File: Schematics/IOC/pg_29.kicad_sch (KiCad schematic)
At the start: 18 parts, among them U2901 F374, U2902 F374, U2903 F374, U2904 F374, U2905 F280, U2906 F280, U2907 F280, U2908 F280, U2909 F374, U2910 F20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

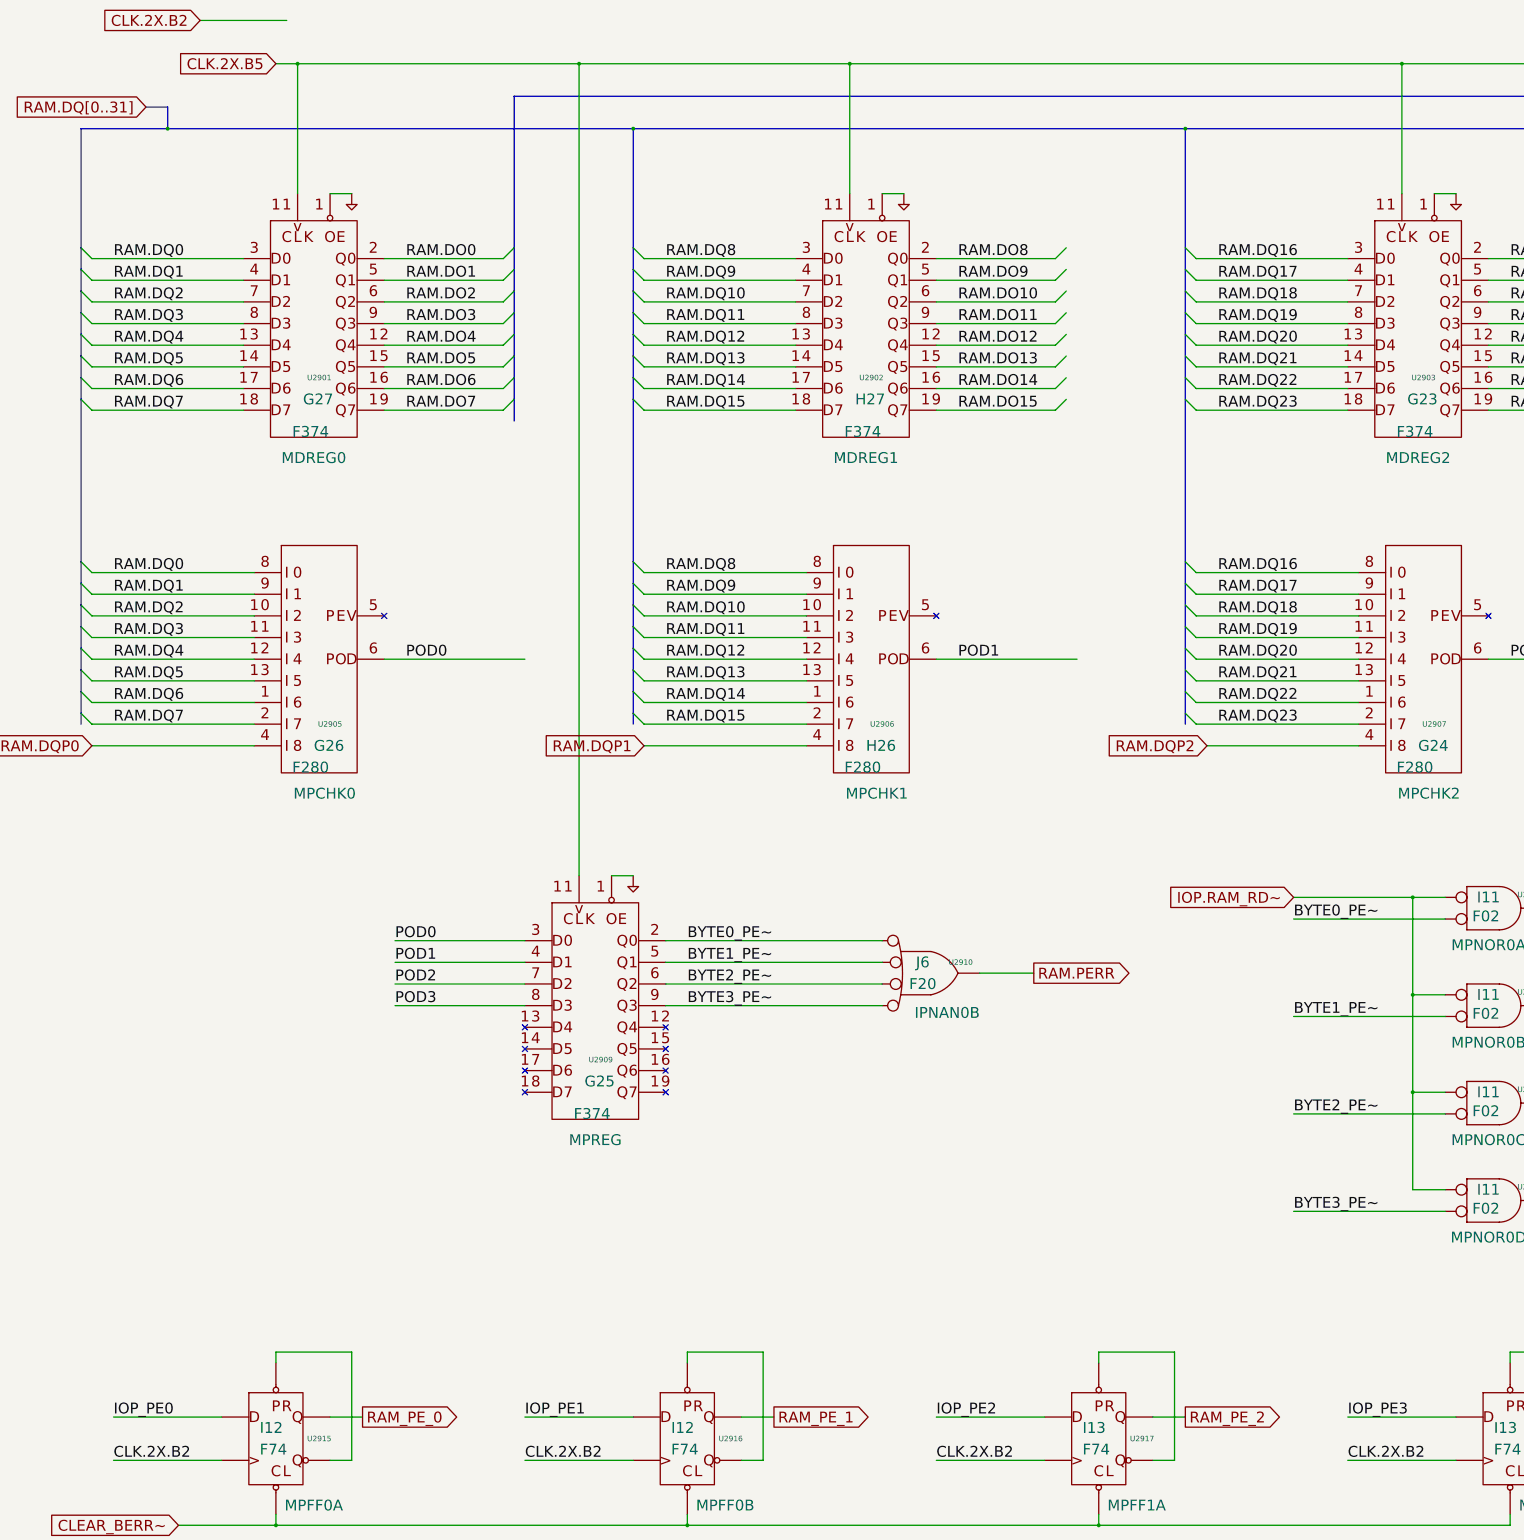
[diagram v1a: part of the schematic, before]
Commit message: Eliminate all multi-buffered signals
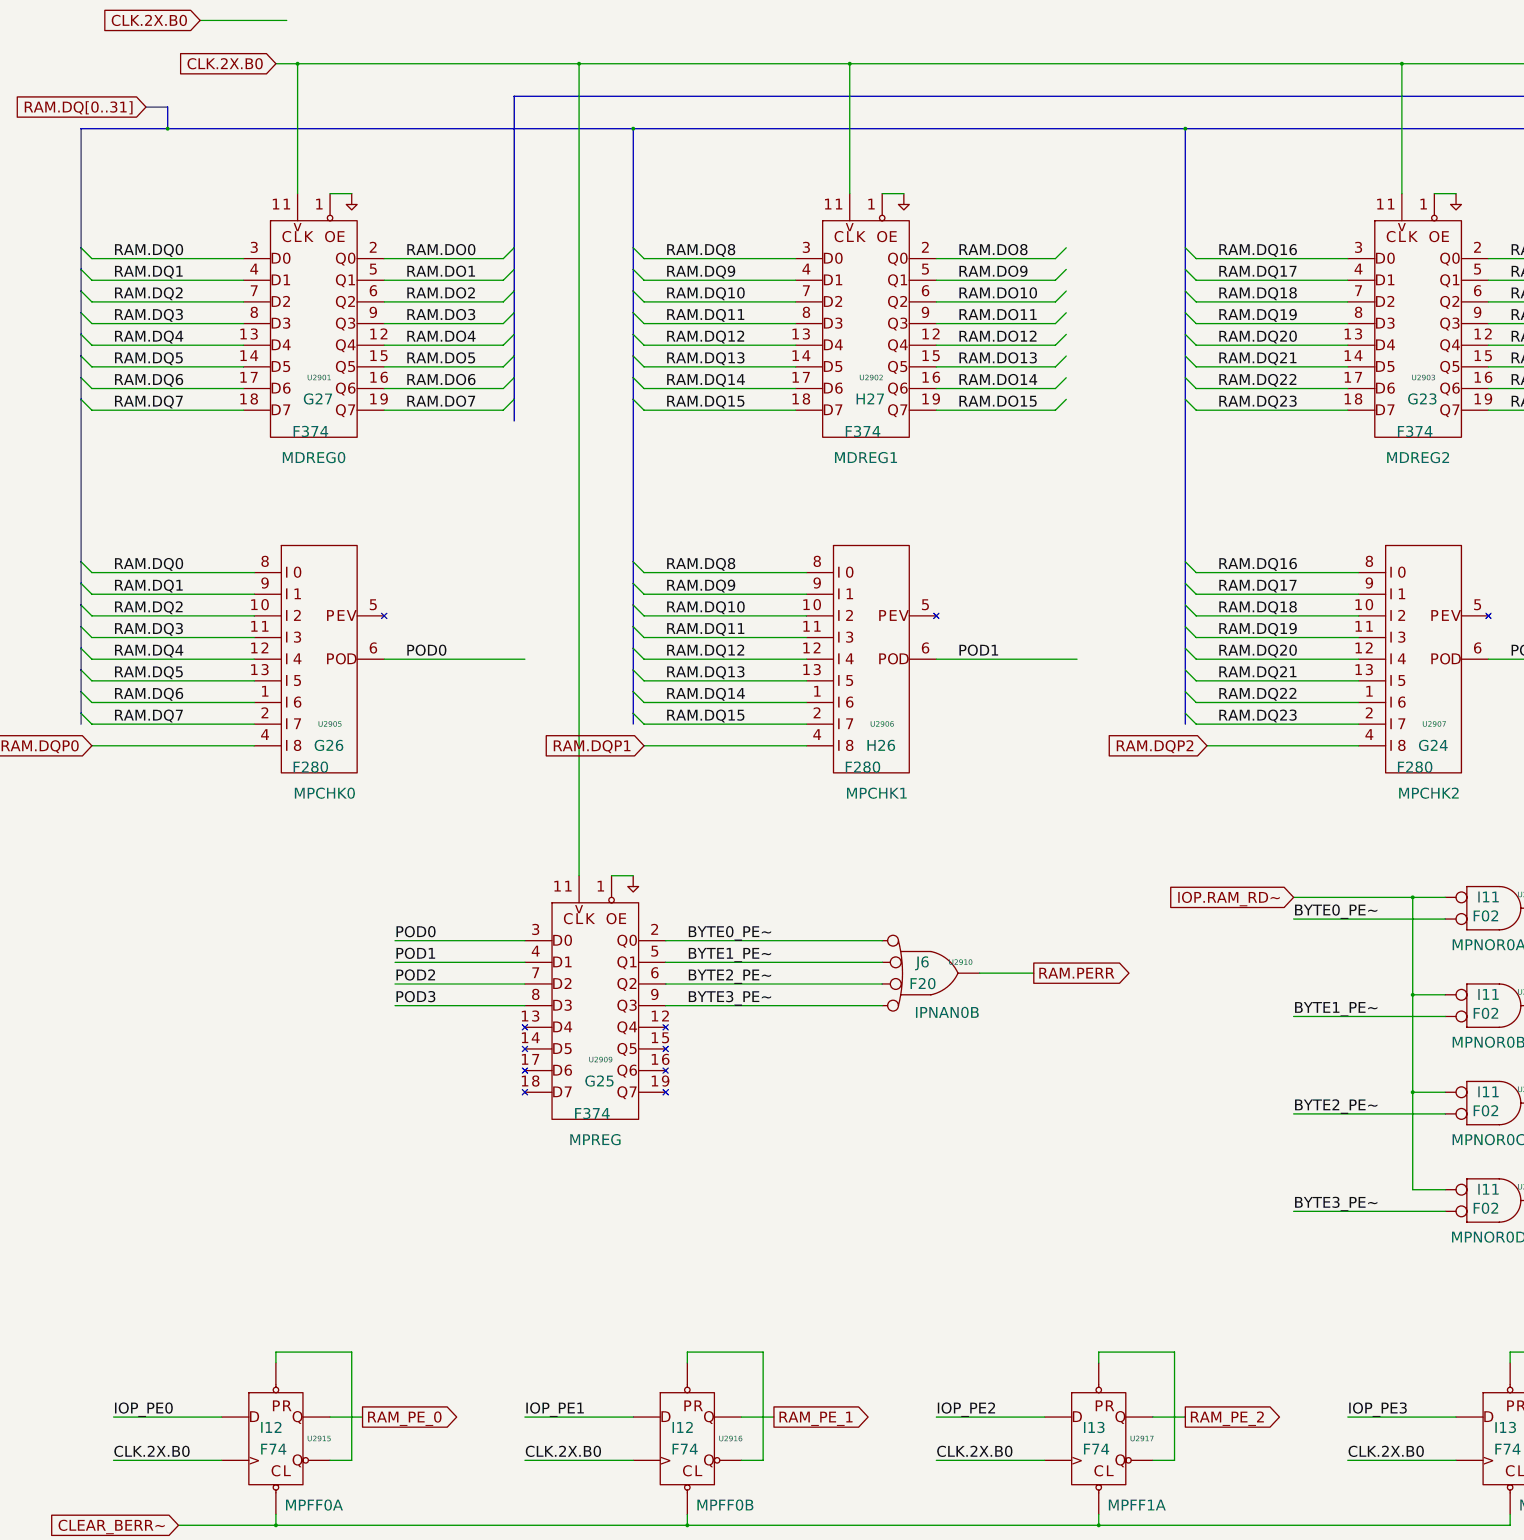
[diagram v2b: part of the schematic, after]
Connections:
- net CLK.2X.B5 is gone; now on net CLK.2X.B0: U2901.11 (CLK), U2902.11 (CLK), U2903.11 (CLK), U2904.11 (CLK), U2909.11 (CLK)
- net CLK.2X.B2 renamed CLK.2X.B0
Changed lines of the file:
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@@
   )
   (label
-    "CLK.2X.B2"
+    "CLK.2X.B0"
     (at 332.74 350.52 0)
     (effects
@@
   )
   (label
-    "CLK.2X.B2"
+    "CLK.2X.B0"
     (at 139.7 350.52 0)
     (effects
@@
   )
   (label
-    "CLK.2X.B2"
+    "CLK.2X.B0"
     (at 236.22 350.52 0)
     (effects
@@
   )
   (label
-    "CLK.2X.B2"
+    "CLK.2X.B0"
     (at 43.18 350.52 0)
     (effects
@@
   )
   (global_label
-    "CLK.2X.B5"
+    "CLK.2X.B0"
     (shape input)
     (at 81.28 22.86 180)
@@
   )
   (global_label
-    "CLK.2X.B2"
+    "CLK.2X.B0"
     (shape input)
     (at 63.5 12.7 180)

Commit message: Replace lots of clock-generation logic with CLKGEN
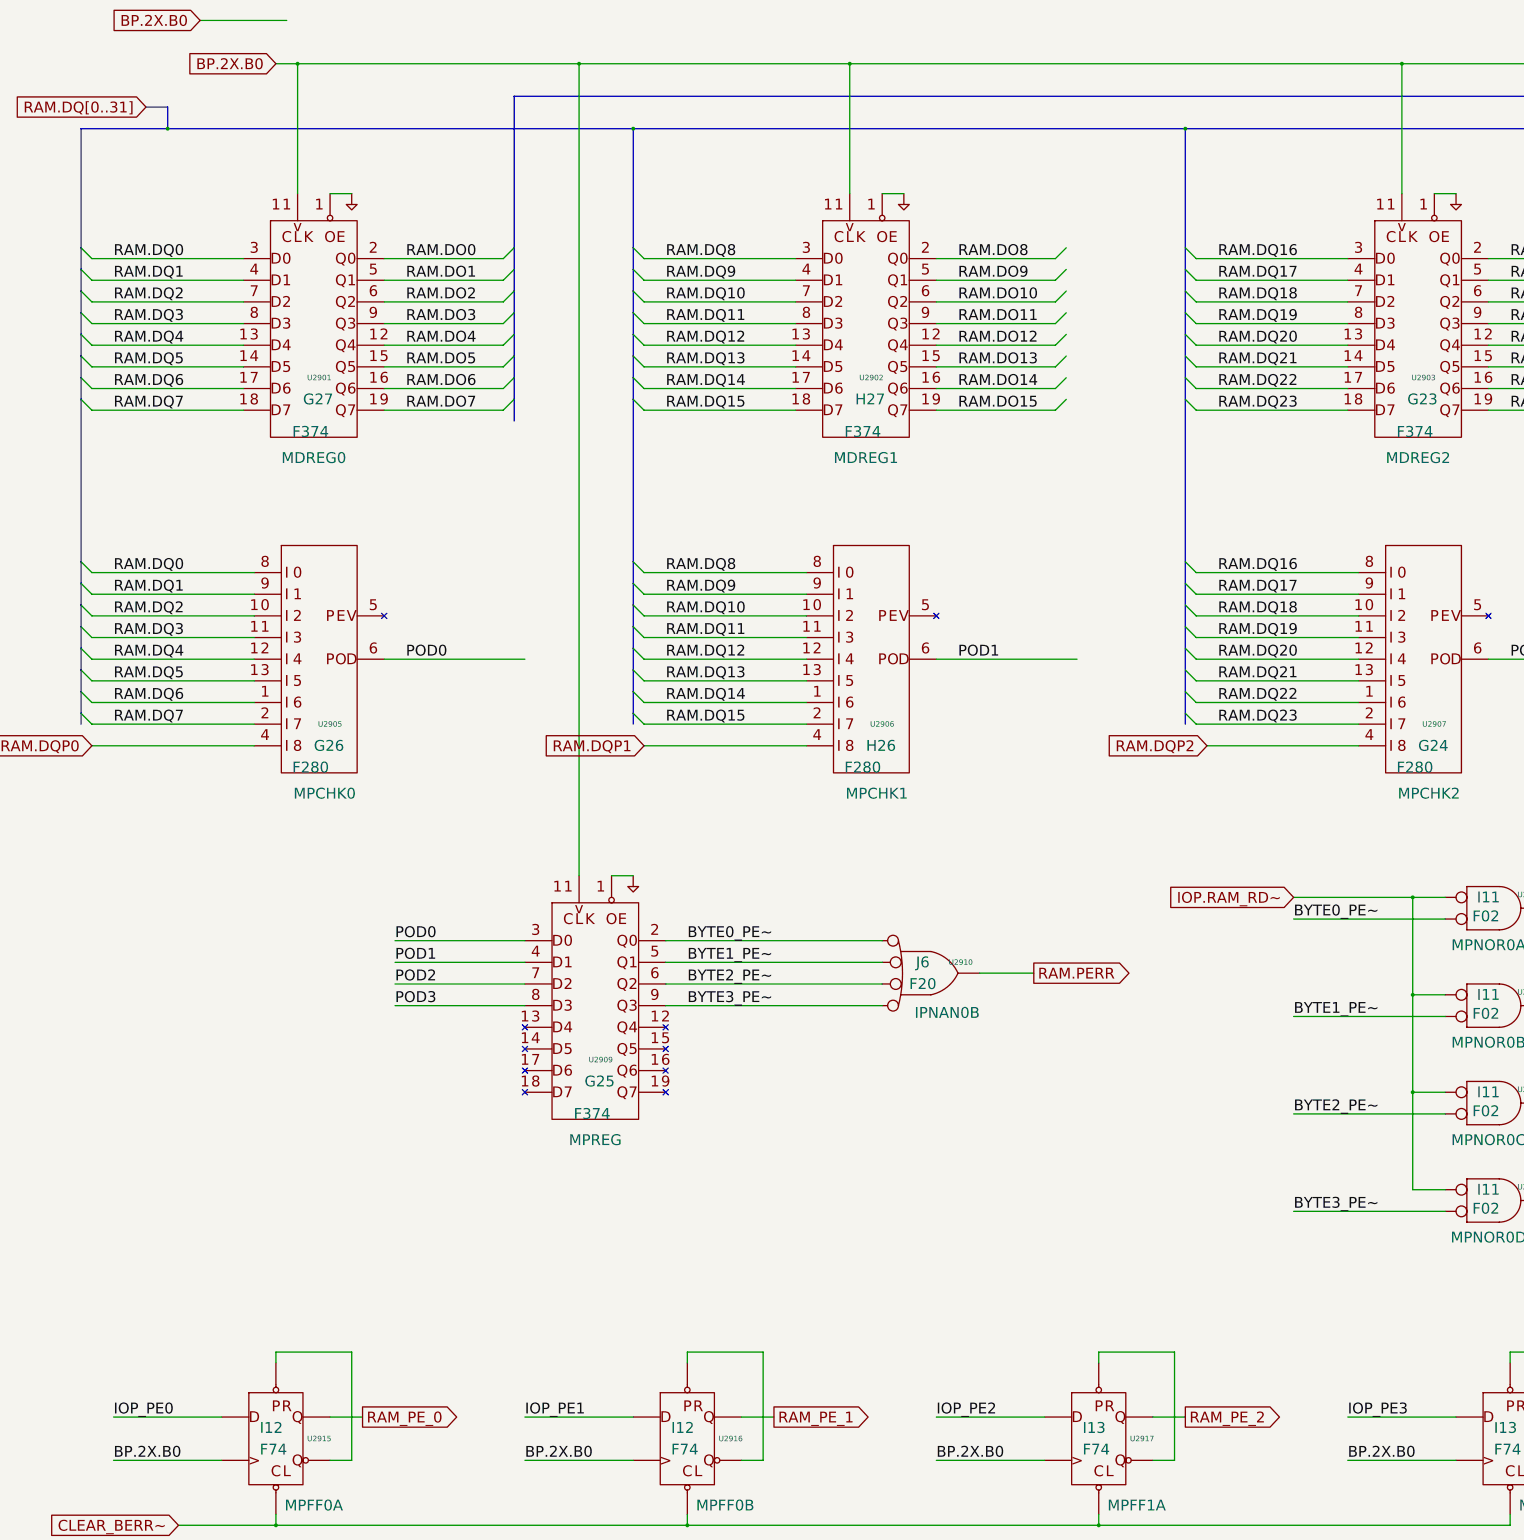
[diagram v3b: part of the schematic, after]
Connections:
- net CLK.2X.B0 renamed BP.2X.B0
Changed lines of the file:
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@@
   )
   (label
-    "CLK.2X.B0"
+    "BP.2X.B0"
     (at 332.74 350.52 0)
     (effects
@@
   )
   (label
-    "CLK.2X.B0"
+    "BP.2X.B0"
     (at 139.7 350.52 0)
     (effects
@@
   )
   (label
-    "CLK.2X.B0"
+    "BP.2X.B0"
     (at 236.22 350.52 0)
     (effects
@@
   )
   (label
-    "CLK.2X.B0"
+    "BP.2X.B0"
     (at 43.18 350.52 0)
     (effects
@@
   )
   (global_label
-    "CLK.2X.B0"
+    "BP.2X.B0"
     (shape input)
     (at 81.28 22.86 180)
@@
   )
   (global_label
-    "CLK.2X.B0"
+    "BP.2X.B0"
     (shape input)
     (at 63.5 12.7 180)
